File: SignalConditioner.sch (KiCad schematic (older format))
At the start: 9 parts, among them IC1 INA152EA_2K5

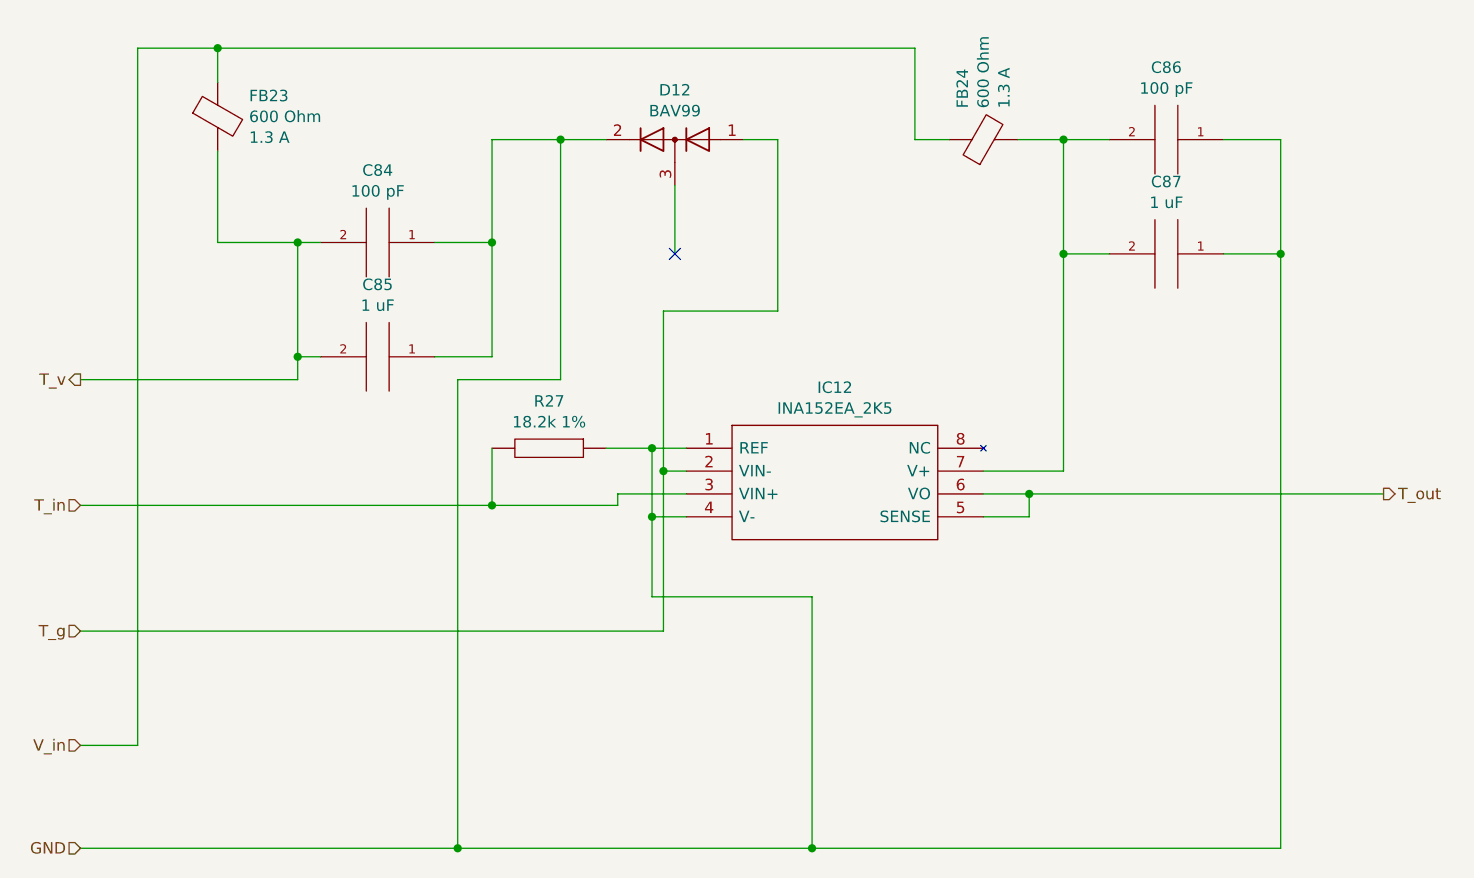
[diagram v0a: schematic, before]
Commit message: Updated Parts
Updated parts to components that are available for order rather than obsolete, out-of-stock, or non-real components.
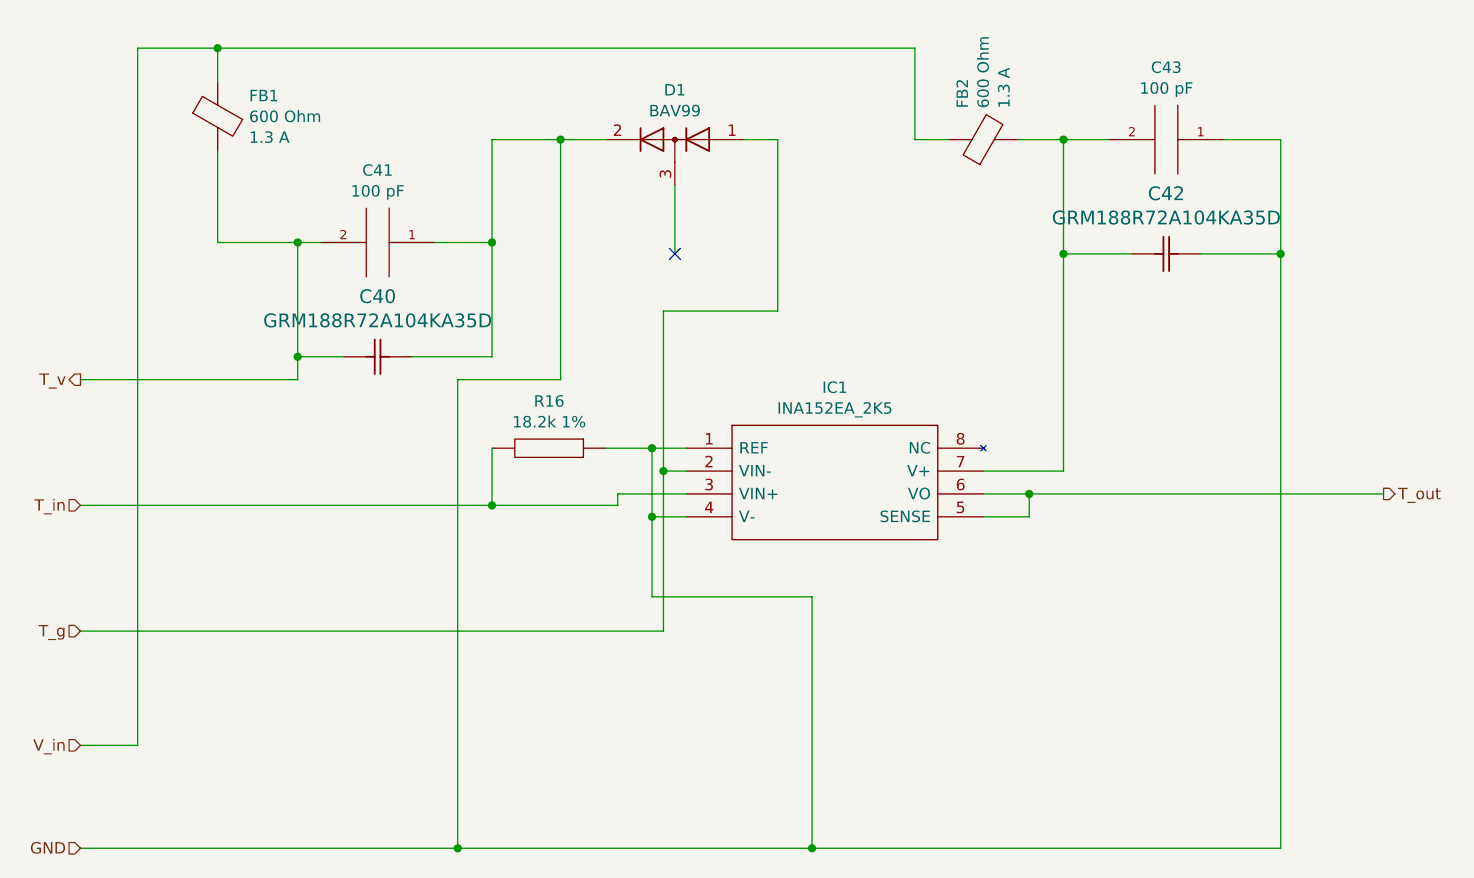
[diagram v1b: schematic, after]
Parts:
- removed C41, C43: 1 uF, symbol pspice:C
- added C40, C42: GRM188R72A104KA35D, G-188_MUR, symbol GRM188R72A104KA35D:GRM188R72A104KA35D
- renumbered C40 to C41, C42 to C43
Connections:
- net GND: now also C40.2, C42.2
- net T_v: now also C40.1
- net at C43.2, FB2.2, IC1.7 (V+): now also C42.1

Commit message: Finished Component Selection
Finished Component selection in schematic and BoM. Ready to design PCB
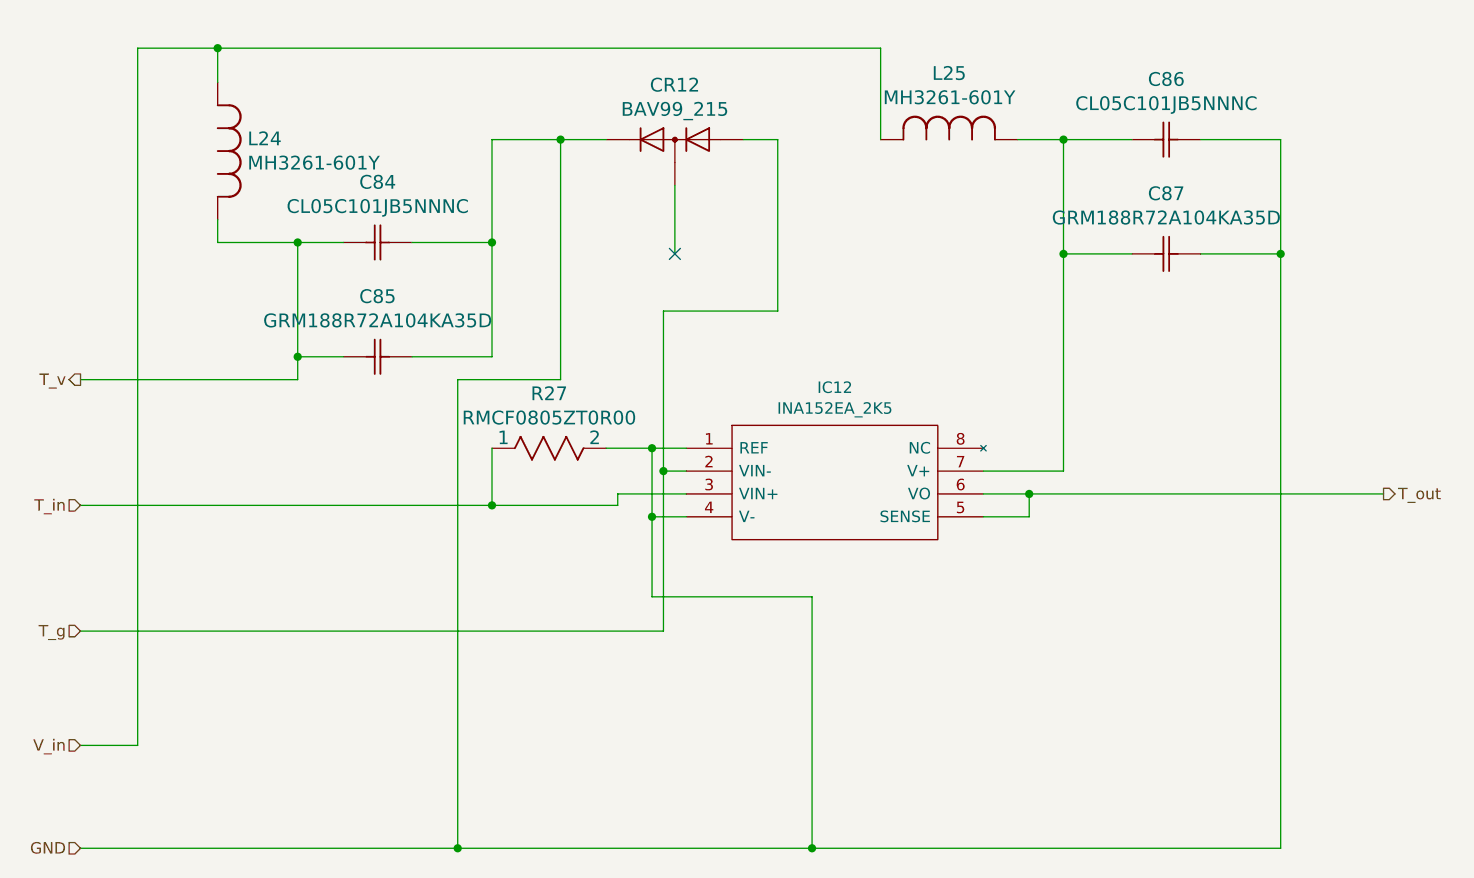
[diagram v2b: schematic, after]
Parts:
- removed C41, C43: 100 pF, symbol pspice:C
- removed D1: BAV99, Package_TO_SOT_SMD:SOT-23, symbol Diode:BAV99
- removed FB1, FB2: Ferrite_Bead, symbol Device:Ferrite_Bead
- removed R16: 18.2k 1%, symbol pspice:R
- added C40, C42: CL05C101JB5NNNC, CAP_CL05_SAM, symbol CL05C101JB5NNNC:CL05C101JB5NNNC
- added CR1: BAV99_215, DIODE_SOT23_BAV99_3X1P4_NEX, symbol BAV99,215:BAV99_215
- added L2, L3: MH3261-601Y, IND_BOURNS_MH3261, symbol MH3261-601Y:MH3261-601Y
- added R16: RMCF0805ZT0R00, STA_RMCF0805_STP, symbol RMCF0805ZT0R00:RMCF0805ZT0R00
- renumbered C40 to C41, C42 to C43
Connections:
- net GND: now also C40.2, C42.2, CR1.2 (A), R16.2
- net T_g: now also CR1.1 (K)
- net T_in: now also R16.1
- net T_v: now also C40.1, L2.1
- net V_in: now also L2.2, L3.2
- net at C43.1, IC1.7 (V+): now also C42.1, L3.1
